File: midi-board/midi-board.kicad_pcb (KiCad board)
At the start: 2 copper layers, 84 x 45 mm, 22 parts, among them J1 MIDI OUT, J2 MIDI IN, J3 UART Header, U1 74LVC1G06, U2 74LVC1G17, U3 TLP185(SE

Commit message: Converted MIDI board to I2C
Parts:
- added C5: 0.1uF, Capacitors_SMD:C_0805_HandSoldering, F.Cu at (151.8, 49.9)
- added C6: 0.1uF, Capacitors_SMD:C_0805_HandSoldering, F.Cu at (163.8, 60.3)
- added C7: 0.1uF, Capacitors_SMD:C_0805_HandSoldering, F.Cu at (144.8, 40.6)
- added C8: 0.1uF, Capacitors_SMD:C_0805_HandSoldering, F.Cu at (171.4, 40.6)
- added FB5: FB, Inductors_SMD:L_0805_HandSoldering, F.Cu at (147.3, 40.6)
- added FB6: FB, Inductors_SMD:L_0805_HandSoldering, F.Cu at (168.9, 40.6)
- added J4: A0, Pin_Headers:Pin_Header_Straight_1x03_Pitch2.54mm, F.Cu at (193.0, 41.8)
- added J5: A1, Pin_Headers:Pin_Header_Straight_1x03_Pitch2.54mm, F.Cu at (182.2, 41.9)
- added J6: Qwiic, Connectors_JST:JST_SH_SM04B-SRSS-TB_04x1.00mm_Angled, F.Cu at (162.9, 40.0)
- added R5: DNP, Resistors_SMD:R_0805_HandSoldering, F.Cu at (196.2, 47.0)
- added R6: DNP, Resistors_SMD:R_0805_HandSoldering, F.Cu at (196.2, 41.9)
- added R7: DNP, Resistors_SMD:R_0805_HandSoldering, F.Cu at (185.4, 47.0)
- added R8: DNP, Resistors_SMD:R_0805_HandSoldering, F.Cu at (185.4, 41.9)
- added R9: DNP, Resistors_SMD:R_0805_HandSoldering, F.Cu at (137.2, 43.9)
- added U4: SC16IS740, Housings_SSOP:TSSOP-16_4.4x5mm_Pitch0.65mm, F.Cu at (159.4, 61.0)
- added X1: SG-5032CAN, Oscillators:Oscillator_SMD_SeikoEpson_SG8002CE-4pin_3.2x2.5mm_HandSoldering, F.Cu at (155.6, 52.1)
- J3: value UART Header -> Qwiic; footprint Pin_Headers:Pin_Header_Angled_1x04_Pitch2.54mm -> Connectors_JST:JST_SH_SM04B-SRSS-TB_04x1.00mm_Angled
- moved C1 4.00 mm to (172.0, 51.5)
- moved FB1 4.00 mm to (186.0, 59.0)
- moved FB2 4.00 mm to (176.0, 59.0)
- moved H3 4.00 mm to (200.0, 72.0)
- moved J1 4.00 mm to (181.0, 77.0)
- moved R1 4.00 mm to (189.5, 56.0)
- moved R3 4.00 mm to (179.5, 56.0)
- moved U1 4.00 mm to (176.0, 51.5)
- moved H2 2.00 mm to (160.0, 72.0)
- moved J3 1.25 mm to (153.7, 40.0), turned to 180 degrees
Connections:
- J3 pad 2: /RX -> Net-(FB5-Pad1)
- J3 pad 3: /TX -> /SDA
- J3 pad 4: +3V3 -> /SCL
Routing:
- net /A0: track 0.00 -> 54.7 mm, vias 0 -> 1
- net /A1: track 0.00 -> 46.6 mm, vias 0 -> 1
- net /SDA: track 0.00 -> 36.9 mm, vias 0 -> 2
- net GND: track 20.2 -> 52.4 mm, vias 4 -> 9
- net /SCL: track 0.00 -> 31.9 mm, vias 0 -> 2
- net /RX: track 17.7 -> 33.4 mm
- net +3V3: track 5.89 -> 19.2 mm
- net Net-(FB5-Pad1): track 0.00 -> 9.12 mm
- net Net-(FB6-Pad1): track 0.00 -> 7.66 mm
- net Net-(R2-Pad2): track 16.2 -> 22.6 mm
- net /TX: track 16.8 -> 22.6 mm
- net Net-(U4-Pad15): track 0.00 -> 4.78 mm
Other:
- board size 84 x 45 mm -> 88 x 45 mm
- board text added: "0"
- board text added: "1"
- board text added: "A0"
- board text added: "A1"
- board text added: "Buffer bypass"
- board text added: "I2C Address Selection Must set"
- board text removed: "+3.3V"
- board text removed: "GND"
- board text removed: "RX ← IN"
- board text removed: "TX → OUT"

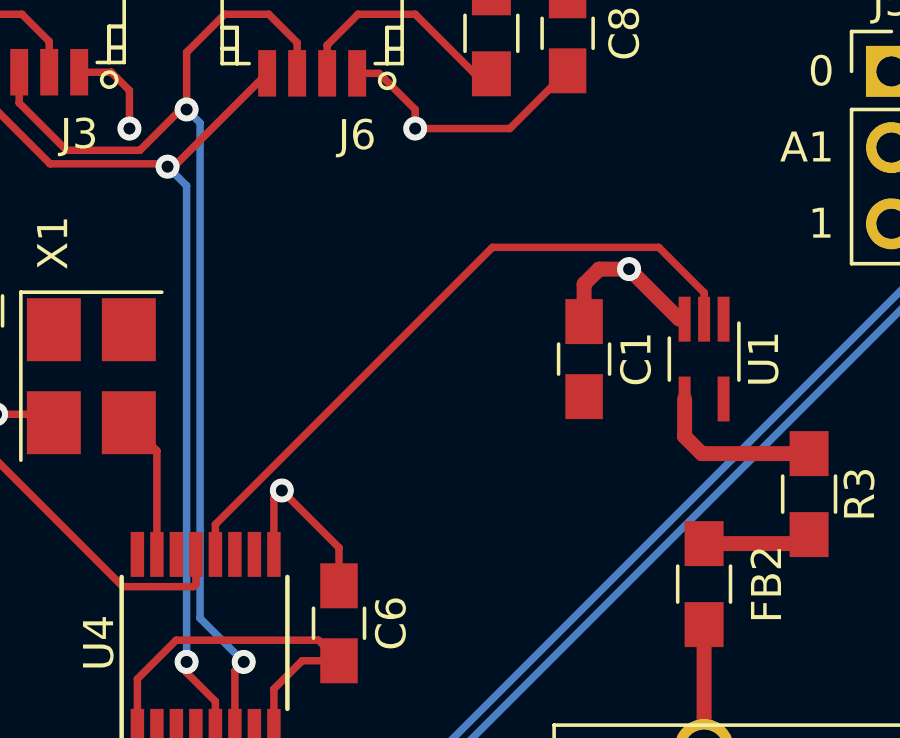
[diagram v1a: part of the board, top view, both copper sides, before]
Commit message: Include a debug header for the TX/RX lines in their TTL state.
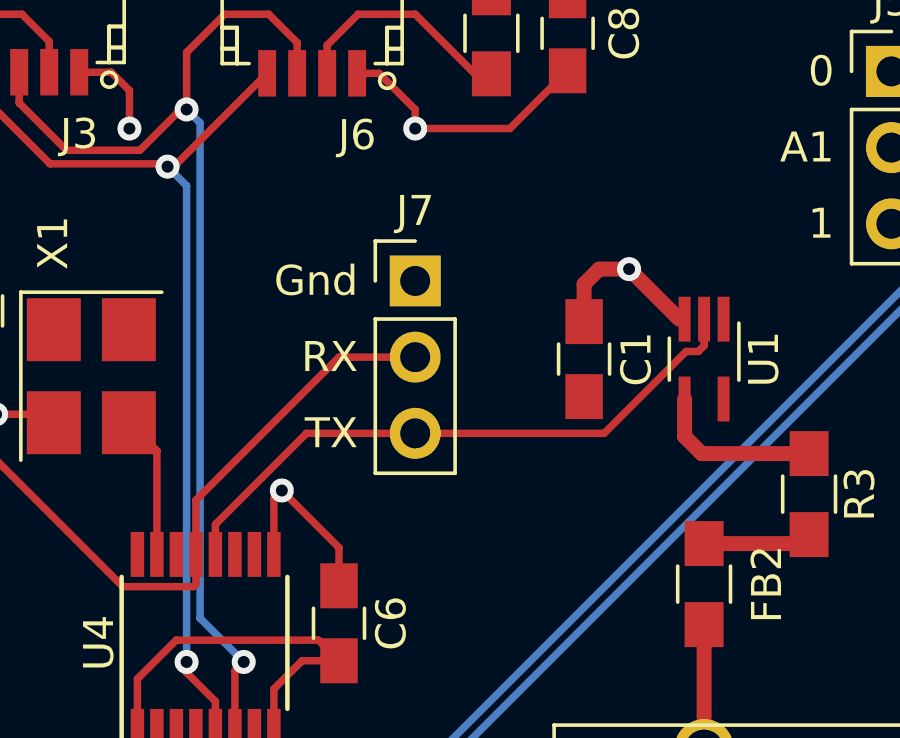
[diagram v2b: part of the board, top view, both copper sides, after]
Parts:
- added J7: UART, Pin_Headers:Pin_Header_Straight_1x03_Pitch2.54mm, F.Cu at (166.4, 48.9)
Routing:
- net /RX: track 33.4 -> 44.5 mm
- net /TX: track 22.6 -> 20.6 mm
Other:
- board text added: "Gnd"
- board text added: "RX"
- board text added: "TX"

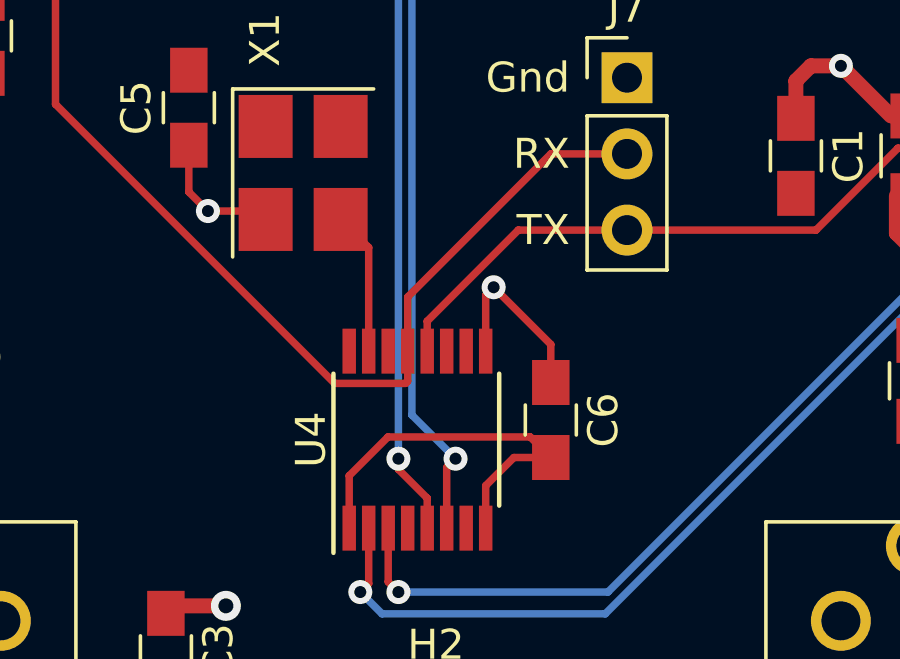
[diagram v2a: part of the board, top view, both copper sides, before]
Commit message: alternate uart symbol for the midi board. not sure why i did this
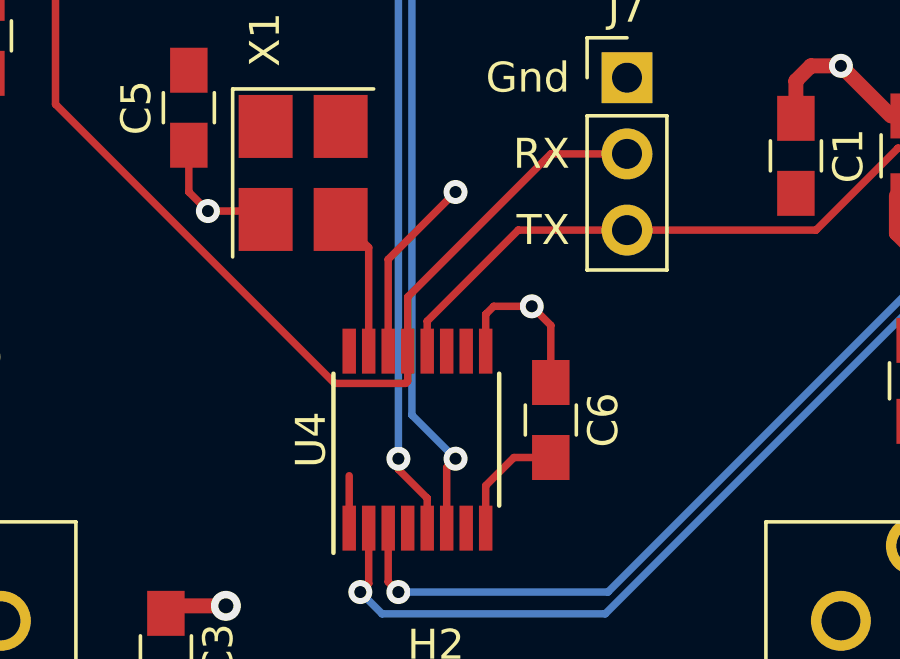
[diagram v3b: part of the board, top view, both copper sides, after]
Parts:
- U4: value SC16IS740 -> SC16IS741AIPW-I2C
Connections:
- net Net-(U4-Pad15) renamed /OSC
- U4 pad 14: (no net) -> +3V3
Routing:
- net +3V3: track 19.2 -> 17.8 mm, vias 0 -> 1
- net GND: track 52.4 -> 51.9 mm
